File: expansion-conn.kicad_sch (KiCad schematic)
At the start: 7 parts, among them J1 J_ERM8-040-XX.X-X-DV-XX_SAMTEC

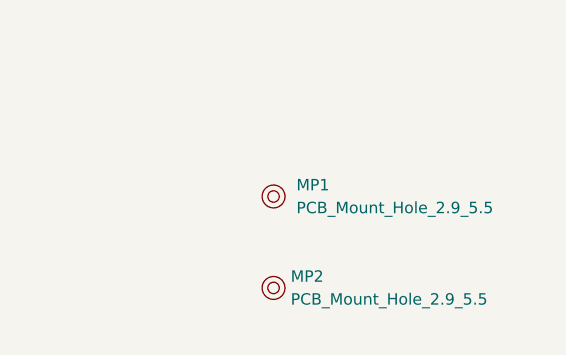
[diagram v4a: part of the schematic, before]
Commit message: [#45990] Fix texts on PCB
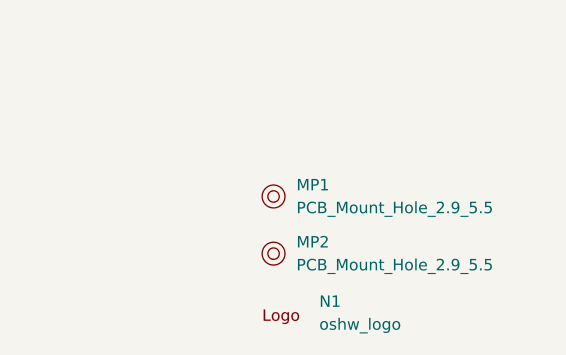
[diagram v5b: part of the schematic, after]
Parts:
- added N1: oshw_logo, antmicro-footprints:oshw-logo, symbol antmicroMechanicalParts:oshw_logo
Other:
- moved on the sheet: MP2
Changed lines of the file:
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@@
     (pin "2")
+  )
+  (symbol (lib_id "antmicroMechanicalParts:oshw_logo") (at 372.11 247.65 0) (unit 1)
+    (in_bom yes) (on_board yes) (fields_autoplaced)
+    (property "Reference" "N1" (id 0) (at 378.46 245.3575 0)
+      (effects (font (size 1.27 1.27) (thickness 0.15)) (justify left))
+    )
+    (property "Value" "oshw_logo" (id 1) (at 378.46 247.8975 0)
+      (effects (font (size 1.27 1.27) (thickness 0.15)) (justify left))
+    )
+    (property "Footprint" "antmicro-footprints:oshw-logo" (id 2) (at 387.35 257.81 0)
+      (effects (font (size 1.27 1.27) (thickness 0.15)) (justify left bottom) hide)
+    )
+    (property "Datasheet" "" (id 3) (at 387.35 260.35 0)
+      (effects (font (size 1.27 1.27) (thickness 0.15)) (justify left bottom) hide)
+    )
+    (property "Author" "Antmicro" (id 4) (at 387.35 262.89 0)
+      (effects (font (size 1.27 1.27) (thickness 0.15)) (justify left bottom) hide)
+    )
+    (property "License" "Apache-2.0" (id 5) (at 387.35 265.43 0)
+      (effects (font (size 1.27 1.27) (thickness 0.15)) (justify left bottom) hide)
+    )
+    (property "MPN" "" (id 6) (at 372.11 247.65 0)
+      (effects (font (size 1.27 1.27)) hide)
+    )
+    (property "Manufacturer" "" (id 7) (at 387.35 267.97 0)
+      (effects (font (size 1.27 1.27) (thickness 0.15)) (justify left bottom) hide)
+    )
   )
   (symbol (lib_id "antmicropower:GND") (at 222.25 182.88 0) (unit 1)
@@
     (pin "1")
   )
-  (symbol (lib_id "antmicroMechanicalParts:PCB_Mount_Hole_2.9_5.5") (at 373.38 243.84 0) (unit 1)
-    (in_bom yes) (on_board yes) (fields_autoplaced)
-    (property "Reference" "MP2" (id 0) (at 375.285 242.5699 0)
-      (effects (font (size 1.27 1.27) (thickness 0.15)) (justify left))
-    )
-    (property "Value" "PCB_Mount_Hole_2.9_5.5" (id 1) (at 375.285 245.1099 0)
-      (effects (font (size 1.27 1.27) (thickness 0.15)) (justify left))
-    )
-    (property "Footprint" "antmicro-footprints:mounting-hole-2.9mm-5.5mm" (id 2) (at 375.92 248.92 0)
-      (effects (font (size 1.27 1.27) (thickness 0.15)) (justify left bottom) hide)
-    )
-    (property "Datasheet" "" (id 3) (at 375.92 251.46 0)
-      (effects (font (size 1.27 1.27) (thickness 0.15)) (justify left bottom) hide)
-    )
-    (property "Author" "Antmicro" (id 4) (at 375.92 254 0)
-      (effects (font (size 1.27 1.27) (thickness 0.15)) (justify left bottom) hide)
-    )
-    (property "License" "Apache-2.0" (id 5) (at 375.92 256.54 0)
-      (effects (font (size 1.27 1.27) (thickness 0.15)) (justify left bottom) hide)
-    )
+  (symbol (lib_id "antmicroMechanicalParts:PCB_Mount_Hole_2.9_5.5") (at 373.38 240.03 0) (unit 1)
+    (in_bom yes) (on_board yes)
+    (property "Reference" "MP2" (id 0) (at 375.92 238.76 0)
+      (effects (font (size 1.27 1.27) (thickness 0.15)) (justify left))
+    )
+    (property "Value" "PCB_Mount_Hole_2.9_5.5" (id 1) (at 375.92 241.3 0)
+      (effects (font (size 1.27 1.27) (thickness 0.15)) (justify left))
+    )
+    (property "Footprint" "antmicro-footprints:mounting-hole-2.9mm-5.5mm" (id 2) (at 375.92 245.11 0)
+      (effects (font (size 1.27 1.27) (thickness 0.15)) (justify left bottom) hide)
+    )
+    (property "Datasheet" "" (id 3) (at 375.92 247.65 0)
+      (effects (font (size 1.27 1.27) (thickness 0.15)) (justify left bottom) hide)
+    )
+    (property "Author" "Antmicro" (id 4) (at 375.92 250.19 0)
+      (effects (font (size 1.27 1.27) (thickness 0.15)) (justify left bottom) hide)
+    )
+    (property "License" "Apache-2.0" (id 5) (at 375.92 252.73 0)
+      (effects (font (size 1.27 1.27) (thickness 0.15)) (justify left bottom) hide)
+    )

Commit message: [#45990] Remove non-sourceable elements from BOMS
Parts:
- MP1, MP2, N1, TP1, TP2, TP3: now left out of the parts list
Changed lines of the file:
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@@
   )
   (symbol (lib_id "antmicroMechanicalParts:oshw_logo") (at 372.11 247.65 0) (unit 1)
-    (in_bom yes) (on_board yes) (fields_autoplaced)
+    (in_bom no) (on_board yes) (fields_autoplaced)
     (property "Reference" "N1" (id 0) (at 378.46 245.3575 0)
       (effects (font (size 1.27 1.27) (thickness 0.15)) (justify left))
@@
   )
   (symbol (lib_id "antmicroMechanicalParts:PCB_Mount_Hole_2.9_5.5") (at 373.38 233.68 0) (mirror y) (unit 1)
-    (in_bom yes) (on_board yes) (fields_autoplaced)
+    (in_bom no) (on_board yes) (fields_autoplaced)
     (property "Reference" "MP1" (id 0) (at 375.92 232.4099 0)
       (effects (font (size 1.27 1.27) (thickness 0.15)) (justify right))
@@
   )
   (symbol (lib_id "antmicroTestPoints:TP_0.75mm_SMD") (at 189.23 180.34 270) (mirror x) (unit 1)
-    (in_bom yes) (on_board yes) (fields_autoplaced)
+    (in_bom no) (on_board yes) (fields_autoplaced)
     (property "Reference" "TP2" (id 0) (at 191.77 177.1649 90)
       (effects (font (size 1.27 1.27) (thickness 0.15)) (justify left))
@@
   )
   (symbol (lib_id "antmicroTestPoints:TP_0.75mm_SMD") (at 132.715 158.75 90) (unit 1)
-    (in_bom yes) (on_board yes) (fields_autoplaced)
+    (in_bom no) (on_board yes) (fields_autoplaced)
     (property "Reference" "TP1" (id 0) (at 134.239 155.5749 90)
       (effects (font (size 1.27 1.27) (thickness 0.15)) (justify right))
@@
   )
   (symbol (lib_id "antmicroTestPoints:TP_0.75mm_SMD") (at 285.75 163.068 90) (unit 1)
-    (in_bom yes) (on_board yes) (fields_autoplaced)
+    (in_bom no) (on_board yes) (fields_autoplaced)
     (property "Reference" "TP3" (id 0) (at 287.274 159.8929 90)
       (effects (font (size 1.27 1.27) (thickness 0.15)) (justify right))
@@
   )
   (symbol (lib_id "antmicroMechanicalParts:PCB_Mount_Hole_2.9_5.5") (at 373.38 240.03 0) (unit 1)
-    (in_bom yes) (on_board yes)
+    (in_bom no) (on_board yes)
     (property "Reference" "MP2" (id 0) (at 375.92 238.76 0)
       (effects (font (size 1.27 1.27) (thickness 0.15)) (justify left))

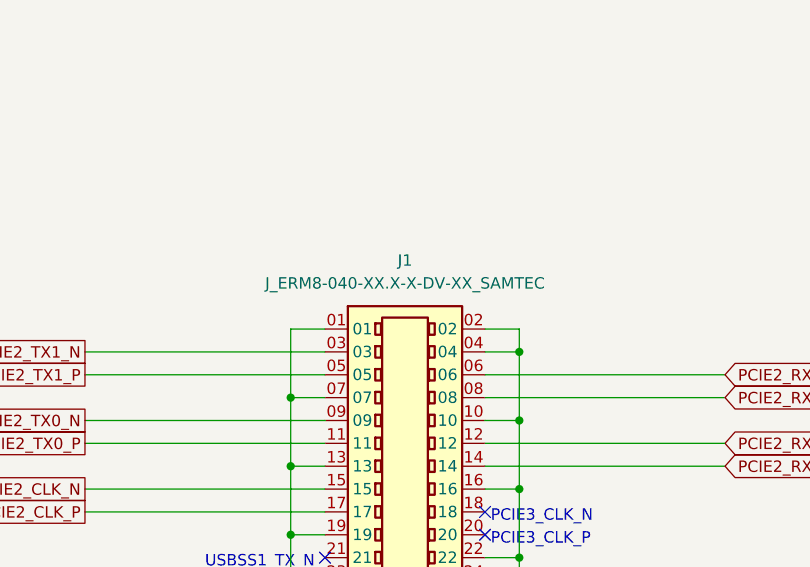
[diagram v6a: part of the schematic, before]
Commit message: Fix MPN and Value on ERM8
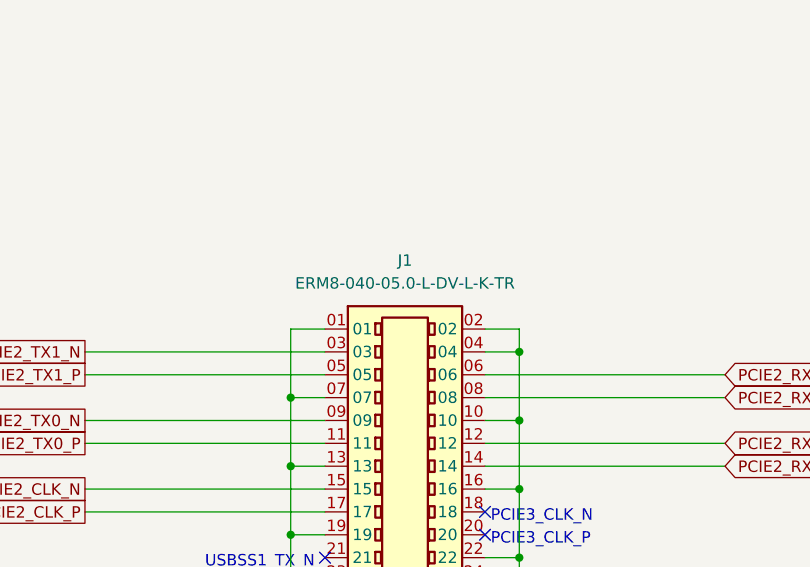
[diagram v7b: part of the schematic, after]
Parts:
- removed J1: J_ERM8-040-XX.X-X-DV-XX_SAMTEC, antmicro-footprints:ERM8-040-05.0_SAMTEC, symbol antmicroB2bConnectors:J_ERM8-040-XX.X-X-DV-XX_SAMTEC
- added J1: J_ERM8-040-05.0-L-DV-L-K-TR_SAMTEC, antmicro-footprints:ERM8-040-05.0_SAMTEC, symbol antmicroB2bConnectors:J_ERM8-040-05.0-L-DV-L-K-TR_SAMTEC
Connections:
- net +3V3: now also J1.67, J1.69
- net 12V_CONN: now also J1.78, J1.80
- net 1V8_CONN: now also J1.73
- net 3V3_STDB: now also J1.74
- net 5V_CONN: now also J1.77, J1.79
- net GND: now also J1.01, J1.02, J1.04, J1.07, J1.10, J1.13, J1.16, J1.19, J1.22, J1.25, J1.28, J1.37, J1.38, J1.49, J1.50, J1.61, J1.62, J1.71, J1.72, J1.75, J1.76
- net PCIE2_CLKREQ: now also J1.29
- net PCIE2_CLK_N: now also J1.15
- net PCIE2_CLK_P: now also J1.17
- net PCIE2_RST: now also J1.27
- net PCIE2_RX0_N: now also J1.12
- net PCIE2_RX0_P: now also J1.14
- net PCIE2_RX1_N: now also J1.06
- net PCIE2_RX1_P: now also J1.08
- net PCIE2_TX0_N: now also J1.09
- net PCIE2_TX0_P: now also J1.11
- net PCIE2_TX1_N: now also J1.03
- net PCIE2_TX1_P: now also J1.05
- net UART1_RXD: now also J1.39
- net USB1_D_N: now also J1.41
- net USB1_D_P: now also J1.43
